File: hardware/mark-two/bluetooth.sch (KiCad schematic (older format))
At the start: 4 parts, among them U11 ANNA-B112

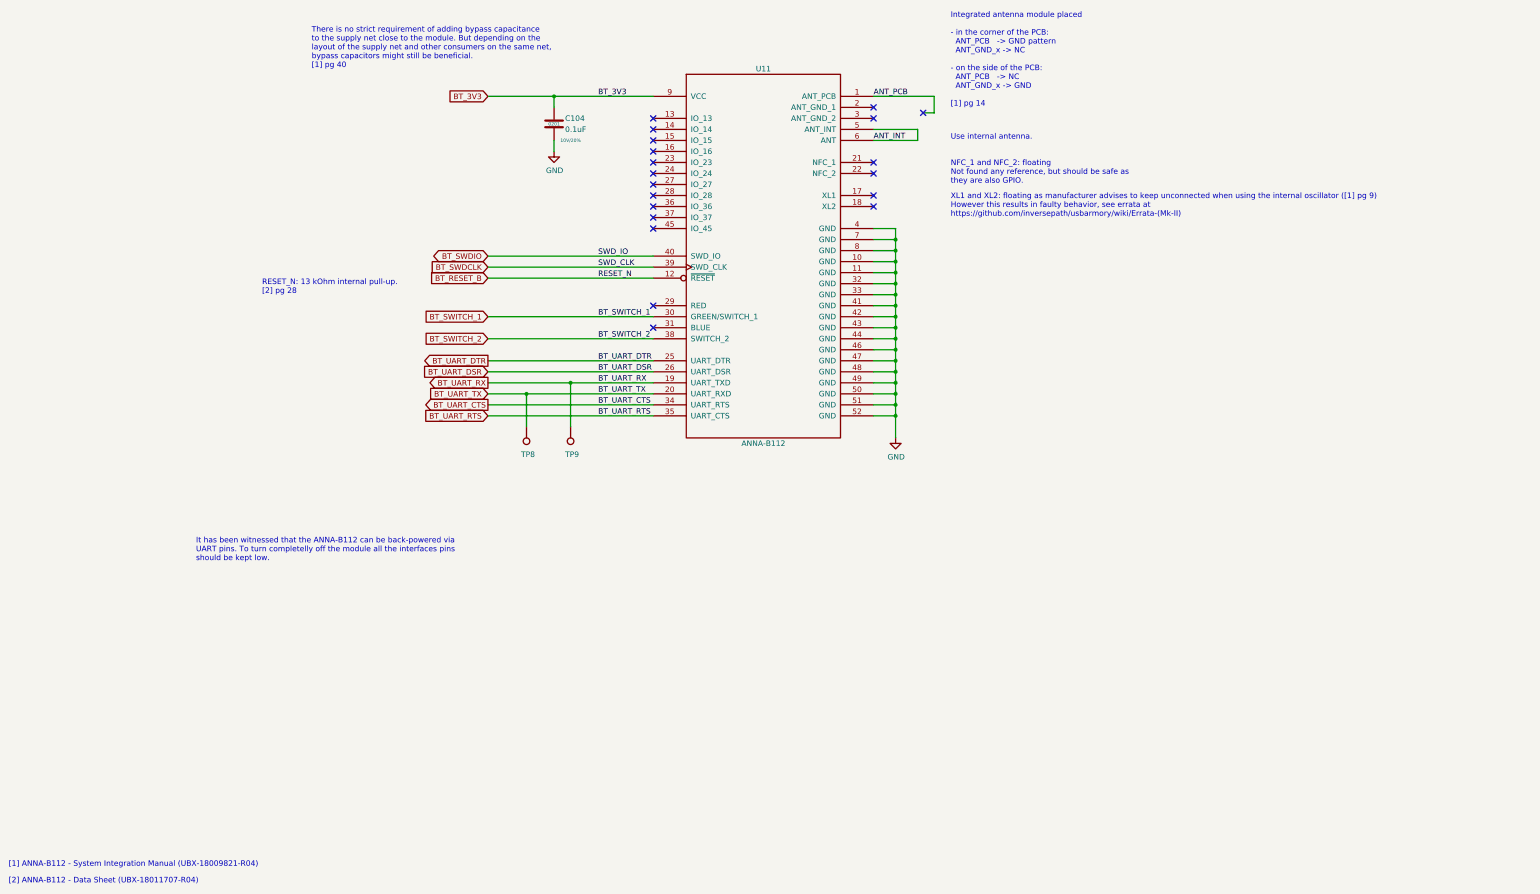
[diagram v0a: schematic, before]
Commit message: add USB armory Mk II rev. γ
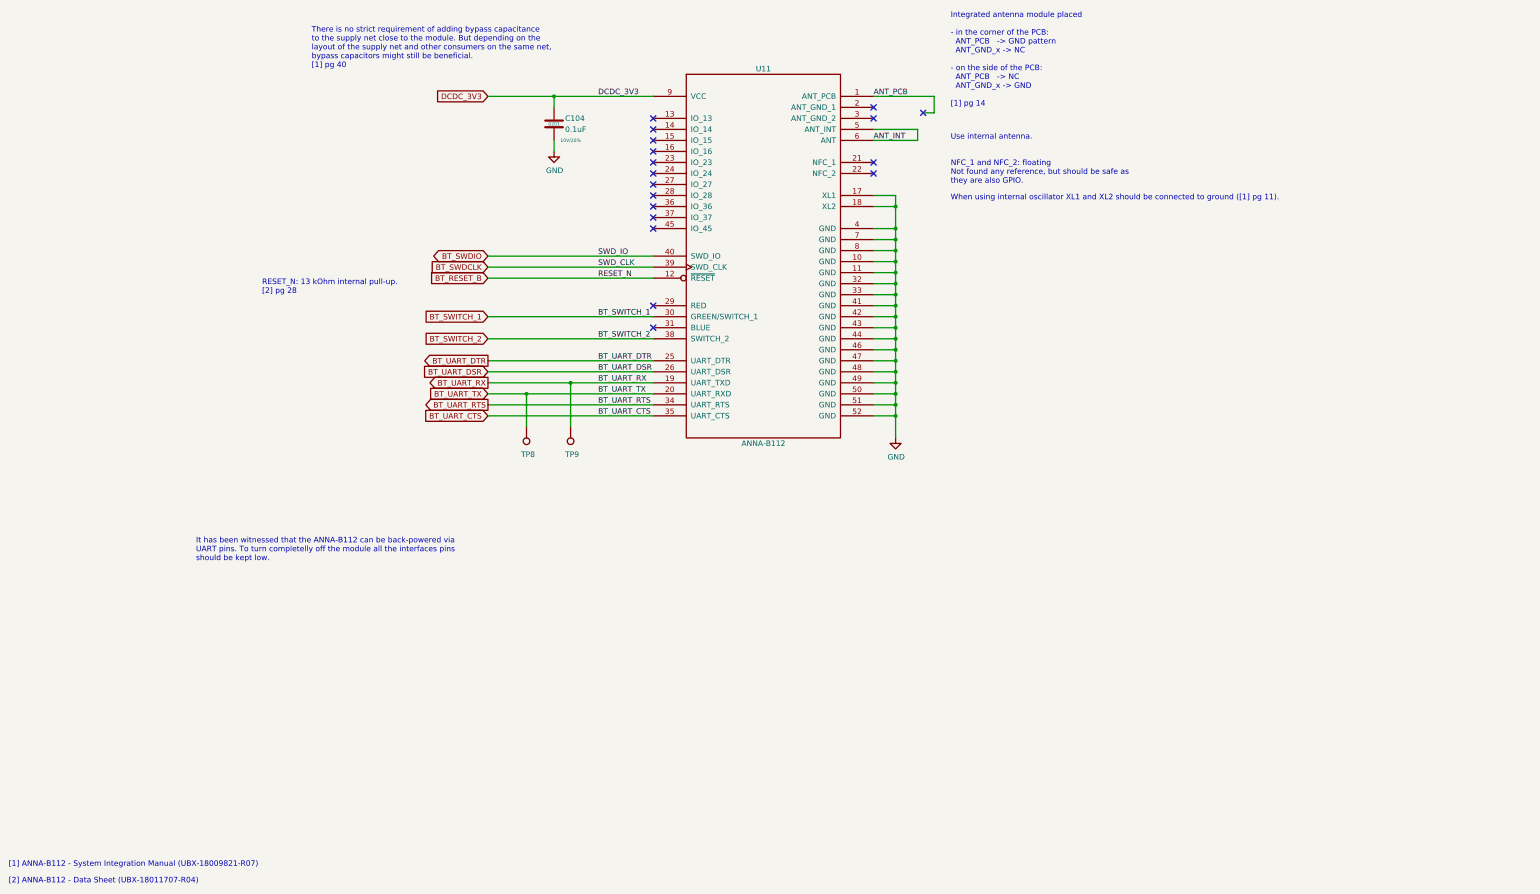
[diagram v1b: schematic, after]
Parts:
- U11: Alternative PN (none) -> ANNA-B112-00B
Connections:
- net BT_UART_CTS: now also U11.35 (UART_CTS); no longer U11.34 (UART_RTS)
- net BT_UART_RTS: now also U11.34 (UART_RTS); no longer U11.35 (UART_CTS)
- net GND: now also U11.17 (XL1), U11.18 (XL2)
- net BT_3V3 renamed DCDC_3V3
- no-connect marks 20 -> 18
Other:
- note added: "When using internal oscillator XL1 and XL2 should be connected to ground ([1] pg 11)."
- note added: "[1] ANNA-B112 - System Integration Manual (UBX-18009821-R07)"
- note removed: "XL1 and XL2: floating as manufacturer advises to keep unconnected when using the internal oscillator ([1] pg 9)\nHowever this results in faulty behavior, see errata at\nhttps://github.com/inversepath/usbarmory/wiki/Errata-(Mk-II)"
- note removed: "[1] ANNA-B112 - System Integration Manual (UBX-18009821-R04)"
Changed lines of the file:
@@
 EESchema Schematic File Version 4
-LIBS:armory-cache
 EELAYER 30 0
 EELAYER END
@@
 encoding utf-8
 Sheet 9 13
-Title "USB ARMORY"
-Date "2019-06-25"
-Rev "MARK II"
+Title "USB armory Mk II"
+Date "2021-02-18"
+Rev "γ"
 Comp "F-Secure"
-Comment1 "Copyright © 2019 F-Secure"
-Comment2 "License: CERN OHL v1.2"
-Comment3 "https://github.com/inversepath/usbarmory"
+Comment1 "Copyright © F-Secure Corporation"
+Comment2 "License: CERN-OHL-S"
+Comment3 "https://github.com/f-secure-foundry/usbarmory"
 Comment4 ""
 $EndDescr
@@
 F 7 "-" H 7900 3550 50  0001 C CNN "Supplier"
 F 8 "-" H 7900 3550 50  0001 C CNN "Supplier PN"
+F 9 "ANNA-B112-00B" H 7900 3550 50  0001 C CNN "Alternative PN"
 	1    7900 3550
 	1    0    0    -1
@@
 	9100 6650 9100 6850
 Text GLabel 5400 3750 0    50   Input ~ 0
-BT_3V3
+DCDC_3V3
 Text Label 6400 3750 0    50   ~ 0
-BT_3V3
+DCDC_3V3
 Text GLabel 5400 6450 0    50   Input ~ 0
 BT_UART_TX
@@
 BT_UART_RX
 Text GLabel 5400 6550 0    50   Output ~ 0
+BT_UART_RTS
+Text GLabel 5400 6650 0    50   Input ~ 0
 BT_UART_CTS
-Text GLabel 5400 6650 0    50   Input ~ 0
-BT_UART_RTS
 Text Label 6400 5200 0    50   ~ 0
 SWD_IO
 Text Label 6400 5300 0    50   ~ 0
 SWD_CLK
-Text Notes 9600 4850 0    50   ~ 0
-XL1 and XL2: floating as manufacturer advises to keep unconnected when using the internal oscillator ([1] pg 9)\nHowever this results in faulty behavior, see errata at\nhttps://github.com/inversepath/usbarmory/wiki/Errata-(Mk-II)
+Text Notes 9600 4700 0    50   ~ 0
+When using internal oscillator XL1 and XL2 should be connected to ground ([1] pg 11).
 Text Notes 9600 4150 0    50   ~ 0
 Use internal antenna.
 Text Notes 1050 10750 0    50   ~ 0
-[1] ANNA-B112 - System Integration Manual (UBX-18009821-R04)
+[1] ANNA-B112 - System Integration Manual (UBX-18009821-R07)
 $Comp
 L power:GND #PWR?
@@
 NoConn ~ 8900 4350
 NoConn ~ 8900 4450
-NoConn ~ 8900 4650
-NoConn ~ 8900 4750
 NoConn ~ 6900 4450
 NoConn ~ 6900 4550
@@
 BT_UART_TX
 Text Label 6400 6550 0    50   ~ 0
+BT_UART_RTS
+Text Label 6400 6650 0    50   ~ 0
 BT_UART_CTS
-Text Label 6400 6650 0    50   ~ 0
-BT_UART_RTS
 Text GLabel 5400 5750 0    50   Input ~ 0
 BT_SWITCH_1
@@
 Text Notes 2750 7975 0    50   ~ 0
 It has been witnessed that the ANNA-B112 can be back-powered via\nUART pins. To turn completelly off the module all the interfaces pins\nshould be kept low.
+Wire Wire Line
+	8900 4750 9100 4750
+Wire Wire Line
+	9100 4750 9100 4950
+Connection ~ 9100 4950
+Wire Wire Line
+	8900 4650 9100 4650
+Wire Wire Line
+	9100 4650 9100 4750
+Connection ~ 9100 4750
 $EndSCHEMATC
